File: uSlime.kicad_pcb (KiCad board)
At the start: 2 copper layers, 26.1 x 21.7 mm, 22 parts, among them U2 AP2112K-3.3TRG1, U3 MCP73831T-2ACI/OT, U4 ESP32-C6FH4, U5 BNO085

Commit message: Modify ESP32
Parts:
- removed U4: ESP32-C6FH4, uSlime-libs:QFN32_ESP32_EXP
- added J1: USB_C_4-LAYER_PADS, Connector_USB:USB_Micro-B_Amphenol_10103594-0001LF_Horizontal, F.Cu at (119.9, 113.9)
- added U1: ESP32-C6-WROOM-1-NARROW, PCM_Espressif:ESP32-C6-MINI-1, F.Cu at (111.8, 92.8)
- BOOT1, RESET1: value MOMENTARY-SWITCH-SPST-SMD-4.6X2.8MM -> SW_Push; footprint Button_Switch_SMD:SW_Push_1P1T_XKB_TS-1187A -> Button_Switch_SMD:SW_SPST_B3U-1000P-B
- moved R5 19.2 mm to (117.7, 105.3)
- moved R6 18.3 mm to (117.7, 107.3)
- moved R1 17.5 mm to (103.9, 96.5), turned to 90 degrees
- moved C3 16.2 mm to (120.6, 103.8)
- moved C2 16.1 mm to (110.4, 102.6)
- moved BOOT1 15.4 mm to (102.9, 92.3), turned to -90 degrees
- moved R3 15.3 mm to (113.2, 110.1)
- moved C4 14.9 mm to (120.7, 105.3)
- moved R4 14.7 mm to (113.2, 111.6)
- moved C5 10.9 mm to (110.2, 110.1)
- moved D1 9.06 mm to (117.4, 103.8), turned to 180 degrees
- moved RESET1 8.89 mm to (120.7, 92.3), turned to -90 degrees
- moved U2 7.86 mm to (119.2, 107.2)
- moved R8 5.97 mm to (104.1, 108.3), turned to 180 degrees
- moved R7 5.48 mm to (103.7, 104.6), turned to 180 degrees
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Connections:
- BOOT1 pad 2: GND -> /ESP32-C6FH4/IO9/BOOT
- C5 pad 2: Net-(U3-VBAT) -> unconnected-(C5-Pad2)
- D2 pad 2: Net-(D2-A) -> unconnected-(D2-A-Pad2)
- R1 pad 2: 3.3V -> +3.3V
- R3 pad 2: Net-(J1-CC2) -> unconnected-(R3-Pad2)
- R4 pad 2: Net-(J1-CC1) -> unconnected-(R4-Pad2)
- R8 pad 2: Net-(U3-STAT) -> unconnected-(R8-Pad2)
- RESET1 pad 2: GND -> /ESP32-C6FH4/ESP_EN
- U2 pad 3: Net-(D1-K) -> unconnected-(U2-EN-Pad3)
- U3 pad 1: Net-(U3-STAT) -> unconnected-(U3-STAT-Pad1)
- U3 pad 2: GND -> unconnected-(U3-VSS-Pad2)
- U3 pad 3: Net-(U3-VBAT) -> unconnected-(U3-VBAT-Pad3)
- U3 pad 4: Net-(D2-A) -> unconnected-(U3-VDD-Pad4)
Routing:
- net /ESP32-C6FH4/ESP_EN: track 0.00 -> 24.5 mm, vias 0 -> 2
- net /ESP32-C6FH4/IO9/BOOT: track 0.00 -> 15.4 mm
- net +3.3V: track 0.00 -> 4.51 mm
- net Net-(D1-A): track 0.00 -> 3.52 mm
- net /ESP32-C6FH4/IO8: track 0.00 -> 2.68 mm
- net Net-(D1-K): track 0.00 -> 1.95 mm
- net Net-(D2-K): track 0.00 -> 1.20 mm
- added copper zone on B.Cu, net GND
- added copper zone on F.Cu, net GND
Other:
- board size 26.1 x 21.7 mm -> 22.2 x 29.6 mm

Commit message: Update PCB
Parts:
- added C6: 0.1 uF, Capacitor_SMD:C_0603_1608Metric, B.Cu at (115.8, 92.1)
- added C7: 22pF, Capacitor_SMD:C_0603_1608Metric, B.Cu at (115.8, 94.6)
- added C8: 22pF, Capacitor_SMD:C_0603_1608Metric, B.Cu at (115.8, 97.1)
- added C9: 0.1 uF, Capacitor_SMD:C_0603_1608Metric, B.Cu at (115.8, 99.6)
- added Y1: 32.768, uSlime-libs:OSC-SMD_L3.2-W1.5, B.Cu at (111.7, 100.1)
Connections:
- U5 pad 10: unconnected-(U5-CLKSEL0-Pad10) -> GND
- U5 pad 11: unconnected-(U5-NRST-Pad11) -> BNO_RST
- U5 pad 17: unconnected-(U5-SA0/H_MOSI-Pad17) -> BNO_MOSI
- U5 pad 18: unconnected-(U5-H_CSN-Pad18) -> BNO_CS
- U5 pad 19: unconnected-(U5-H_SCL/SCK/RX-Pad19) -> BNO_SCL
- U5 pad 2: unconnected-(U5-GND-Pad2) -> GND
- U5 pad 20: unconnected-(U5-H_SDA/H_MISO/TX-Pad20) -> BNO_SDA
- U5 pad 25: unconnected-(U5-GND-Pad25) -> GND
- U5 pad 26: unconnected-(U5-XOUT32/CLKSEL1-Pad26) -> Net-(U5-XOUT32/CLKSEL1)
- U5 pad 27: unconnected-(U5-XIN32-Pad27) -> Net-(U5-XIN32)
- U5 pad 28: unconnected-(U5-VDDIO-Pad28) -> +3.3V
- U5 pad 3: unconnected-(U5-VDD-Pad3) -> +3.3V
- U5 pad 9: unconnected-(U5-CAP-Pad9) -> Net-(U5-CAP)

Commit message: update power
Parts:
- removed BOOT1: SW_Push, Button_Switch_SMD:SW_SPST_B3U-1000P-B
- added CHRG1: LED, LED_SMD:LED_0402_1005Metric, F.Cu at (102.9, 90.6)
- added U4: S2B-PH-K-S-GW, Connector_JST:JST_PH_S2B-PH-K_1x02_P2.00mm_Horizontal, F.Cu at (116.9, 112.2)
- added U6: MSK-12C02_SMD_SPDT_SWITCH, uSlime-libs:SW_PCM12SMTR, F.Cu at (128.9, 104.8)
- D1: footprint LED_SMD:LED_0402_1005Metric -> Diode_SMD:D_0603_1608Metric
- J1: value USB_C_4-LAYER_PADS -> USB_B_Micro
- R5: value 100k -> 390
- R6: value 390 -> 10K
- R7: value R -> 100K
- U5: moved to F.Cu
- moved U5 20.2 mm to (104.2, 114.3), turned to 0 degrees
- moved C1 7.50 mm to (129.2, 96.4)
- moved R2 7.50 mm to (127.2, 96.4)
- moved RESET1 7.50 mm to (128.2, 92.2)
- moved J1 6.69 mm to (126.5, 114.8)
- moved R6 4.57 mm to (120.4, 103.6)
- moved C5 3.95 mm to (108.9, 106.3)
- moved R3 3.95 mm to (111.9, 106.3)
- moved R4 3.95 mm to (111.9, 107.8)
- moved R5 1.28 mm to (117.4, 106.6)
- moved C4 1.28 mm to (120.4, 106.6)
- moved C3 1.27 mm to (120.4, 105.1)
- moved D1 1.25 mm to (117.4, 105.1)
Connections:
- C3 pad 1: Net-(D1-K) -> VBAT
- C4 pad 1: Net-(U2-VOUT) -> 3.3V
- C5 pad 1: unconnected-(C5-Pad1) -> GND
- C5 pad 2: unconnected-(C5-Pad2) -> VBAT
- C6 pad 1: unconnected-(C6-Pad1) -> GND
- D1 pad 1: Net-(D1-K) -> VBAT
- D1 pad 2: Net-(D1-A) -> VBUS
- J1 pad 1: V_USB -> VBUS
- J1 pad 2: /ESP32-C6FH4/USB_N -> D+ P
- J1 pad 3: /ESP32-C6FH4/USB_P -> D- N
- R5 pad 1: Net-(D1-A) -> VBUS
- R6 pad 1: Net-(D1-A) -> VBAT
- R6 pad 2: unconnected-(R6-Pad2) -> GND
- R7 pad 1: GND -> VBUS
- R7 pad 2: unconnected-(R7-Pad2) -> GND
- R8 pad 1: Net-(D2-K) -> Net-(CHRG1-K)
- R8 pad 2: unconnected-(R8-Pad2) -> Net-(U3-STAT)
- U1 pad 13: /ESP32-C6FH4/USB_N -> D- N
- U1 pad 14: /ESP32-C6FH4/USB_P -> D+ P
- U2 pad 1: Net-(D1-K) -> VBAT
- U2 pad 3: unconnected-(U2-EN-Pad3) -> VBAT
- U2 pad 5: Net-(U2-VOUT) -> 3.3V
- U3 pad 1: unconnected-(U3-STAT-Pad1) -> Net-(U3-STAT)
- U3 pad 2: unconnected-(U3-VSS-Pad2) -> GND
- U3 pad 3: unconnected-(U3-VBAT-Pad3) -> VBAT
- U3 pad 4: unconnected-(U3-VDD-Pad4) -> VBUS
- U3 pad 5: unconnected-(U3-PROG-Pad5) -> Net-(U3-PROG)
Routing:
- net /ESP32-C6FH4/IO9/BOOT: track 15.4 -> 2.26 mm
- net Net-(D1-A): track 3.52 -> 0.00 mm
- net VBAT: track 0.00 -> 1.95 mm
- net Net-(D1-K): track 1.95 -> 0.00 mm
- net VBUS: track 0.00 -> 1.52 mm
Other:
- board size 22.2 x 29.6 mm -> 30 x 30 mm

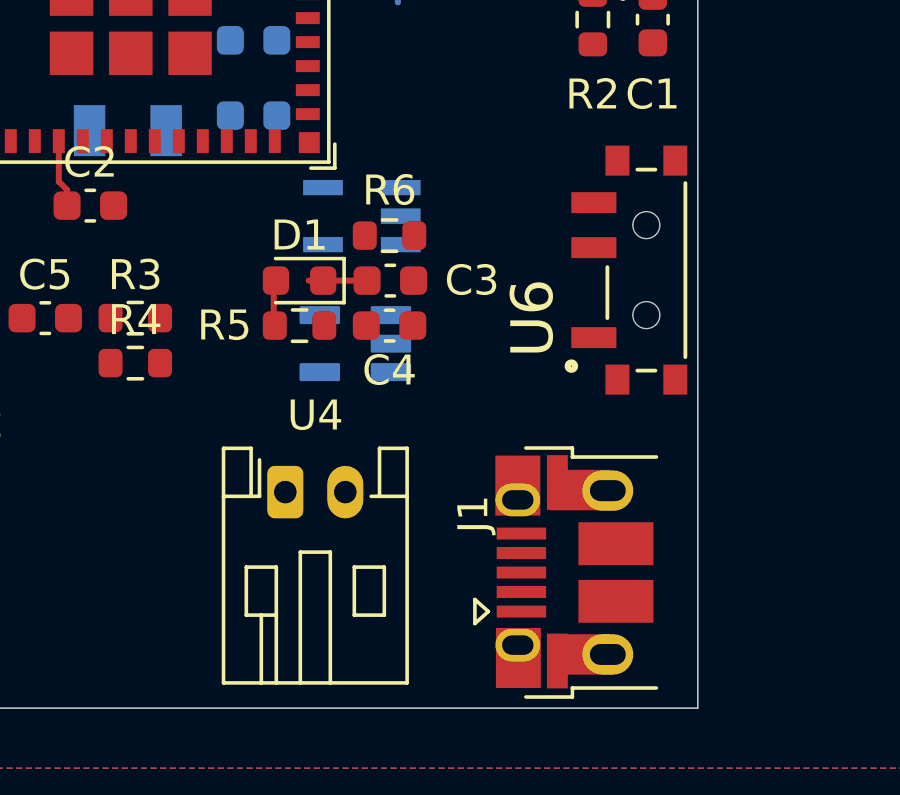
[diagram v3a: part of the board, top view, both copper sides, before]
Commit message: Modify ESP32 connections
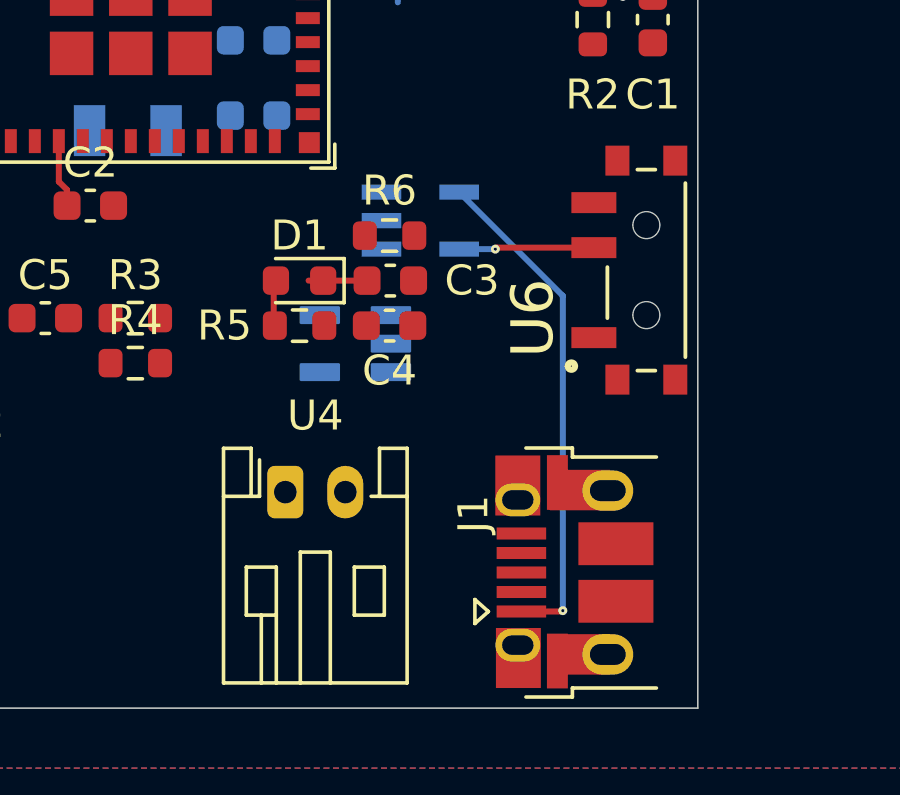
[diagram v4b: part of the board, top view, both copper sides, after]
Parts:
- moved U3 1.96 mm to (121.4, 103.1), turned to 0 degrees
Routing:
- net VBUS: track 1.52 -> 18.3 mm, vias 0 -> 1
- net Net-(U3-PROG): track 0.00 -> 4.51 mm, vias 0 -> 1

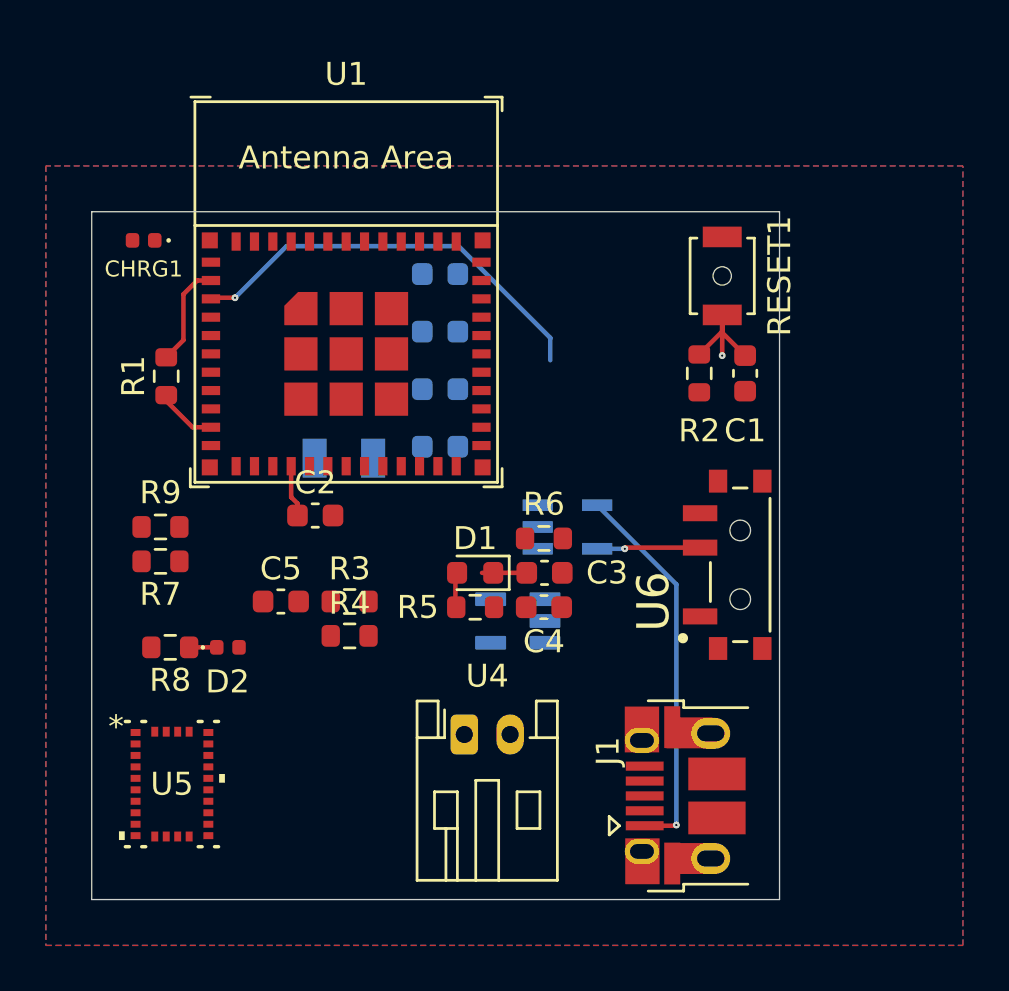
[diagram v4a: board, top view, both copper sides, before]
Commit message: Replace ESP32 symbol with right ESP32
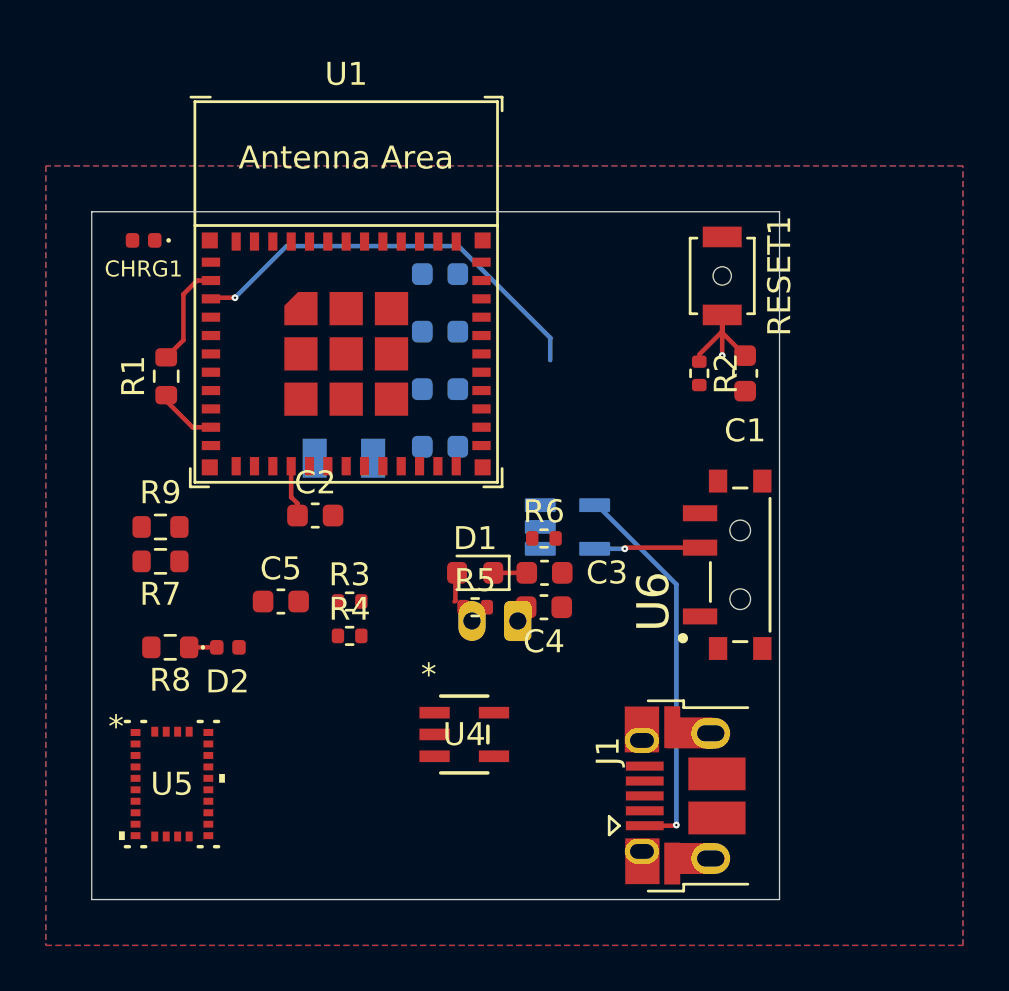
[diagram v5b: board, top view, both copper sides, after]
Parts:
- R2: footprint Resistor_SMD:R_0603_1608Metric -> Resistor_SMD:R_0402_1005Metric
- R3: value 5.1k -> 100K; footprint Resistor_SMD:R_0603_1608Metric -> Resistor_SMD:R_0402_1005Metric
- R4: value 5.1k -> 1k; footprint Resistor_SMD:R_0603_1608Metric -> Resistor_SMD:R_0402_1005Metric
- R5: value 390 -> 4.7k; footprint Resistor_SMD:R_0603_1608Metric -> Resistor_SMD:R_0402_1005Metric
- R6: value 10K -> 100KOHM-0402T-1/16W-1%; footprint Resistor_SMD:R_0603_1608Metric -> Resistor_SMD:R_0402_1005Metric
- U1: value ESP32-C6-WROOM-1-NARROW -> ESP32-C6-MINI-1
- U2: value AP2112K-3.3TRG1 -> S2B-PH-K-S-GW; footprint uSlime-libs:SOT95P285X140-5N -> Connector_JST:JST_PH_S2B-PH-K_1x02_P2.00mm_Horizontal
- U3: value MCP73831T-2ACI/OT -> AP2112K-3.3TRG1; footprint uSlime-libs:SOT-23-5_MC_MCH -> uSlime-libs:SOT95P285X140-5N
- U4: value S2B-PH-K-S-GW -> MCP73831T-2ACI/OT; footprint Connector_JST:JST_PH_S2B-PH-K_1x02_P2.00mm_Horizontal -> uSlime-libs:SOT-23-5_MC_MCH
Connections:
- C4 pad 1: 3.3V -> +3.3V
- R2 pad 2: 3.3V -> +3.3V
- R3 pad 1: GND -> VBUS
- R3 pad 2: unconnected-(R3-Pad2) -> GND
- R4 pad 1: GND -> Net-(CHRG1-K)
- R4 pad 2: unconnected-(R4-Pad2) -> Net-(U4-STAT)
- R5 pad 1: VBUS -> GND
- R5 pad 2: GND -> unconnected-(R5-Pad2)
- R6 pad 1: VBAT -> /ESP32-C6FH4/IO8
- R6 pad 2: GND -> +3.3V
- U1 pad 10: /ESP32-C6FH4/IO8 -> /ESP32-C6FH4/IO5
- U1 pad 11: /ESP32-C6FH4/IO10 -> GND
- U1 pad 12: /ESP32-C6FH4/IO11/~{ALRT} -> /ESP32-C6FH4/IO0
- U1 pad 13: D- N -> /ESP32-C6FH4/IO1/V_BATT_2
- U1 pad 14: D+ P -> GND
- U1 pad 15: /ESP32-C6FH4/IO9/BOOT -> BNO_SDA
- U1 pad 16: /ESP32-C6FH4/IO18/~{CS} -> BNO_SCL
- U1 pad 17: /ESP32-C6FH4/IO19/SCK -> D- N
- U1 pad 18: /ESP32-C6FH4/IO20/PICO -> D+ P
- U1 pad 19: /ESP32-C6FH4/IO21/POCI -> /ESP32-C6FH4/IO14
- U1 pad 2: +3.3V -> GND
- U1 pad 20: /ESP32-C6FH4/IO22/~{SD_DET} -> /ESP32-C6FH4/IO15/LP
- U1 pad 21: /ESP32-C6FH4/IO23/STAT -> (no net)
- U1 pad 22: (no net) -> /ESP32-C6FH4/IO8
- U1 pad 23: /ESP32-C6FH4/IO15/LP -> /ESP32-C6FH4/IO9/BOOT
- U1 pad 24: /ESP32-C6FH4/IO17/RX -> BNO_CS
- U1 pad 25: /ESP32-C6FH4/IO16/TX -> BNO_MOSI
- U1 pad 26: /ESP32-C6FH4/IO3 -> /ESP32-C6FH4/IO20/PICO
- U1 pad 27: /ESP32-C6FH4/IO2 -> /ESP32-C6FH4/IO21/POCI
- U1 pad 28: GND -> /ESP32-C6FH4/IO22/~{SD_DET}
- U1 pad 29: GND -> /ESP32-C6FH4/IO23/STAT
- U1 pad 3: /ESP32-C6FH4/ESP_EN -> +3.3V
- U1 pad 30: GND -> /ESP32-C6FH4/IO17/RX
- U1 pad 31: GND -> /ESP32-C6FH4/IO16/TX
- U1 pad 32: GND -> (no net)
- U1 pad 33: GND -> (no net)
- U1 pad 34: GND -> (no net)
- U1 pad 35: GND -> (no net)
- U1 pad 38: (no net) -> GND
- U1 pad 39: (no net) -> GND
- U1 pad 4: /ESP32-C6FH4/IO4 -> (no net)
- U1 pad 40: (no net) -> GND
- U1 pad 41: (no net) -> GND
- U1 pad 42: (no net) -> GND
- U1 pad 43: (no net) -> GND
- U1 pad 44: (no net) -> GND
- U1 pad 45: (no net) -> GND
- U1 pad 46: (no net) -> GND
- U1 pad 47: (no net) -> GND
- U1 pad 48: (no net) -> GND
- U1 pad 49: (no net) -> GND
- U1 pad 5: /ESP32-C6FH4/IO5 -> /ESP32-C6FH4/IO2
- U1 pad 50: (no net) -> GND
- U1 pad 51: (no net) -> GND
- U1 pad 52: (no net) -> GND
- U1 pad 53: (no net) -> GND
- U1 pad 6: /ESP32-C6FH4/IO6/SDA -> /ESP32-C6FH4/IO3
- U1 pad 7: /ESP32-C6FH4/IO7/SCL -> (no net)
- U1 pad 8: /ESP32-C6FH4/IO0 -> /ESP32-C6FH4/ESP_EN
- U1 pad 9: /ESP32-C6FH4/IO1 -> /ESP32-C6FH4/IO4
- U3 pad 1: Net-(U3-STAT) -> VBAT
- U3 pad 4: VBUS -> (no net)
- U3 pad 5: Net-(U3-PROG) -> +3.3V
- U4 pad 1: VBAT -> Net-(U4-STAT)
- U6 pad COM: Net-(U3-PROG) -> Net-(U4-PROG)
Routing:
- net /ESP32-C6FH4/ESP_EN: track 24.5 -> 6.10 mm, vias 2 -> 1
- net +3.3V: track 4.51 -> 22.9 mm, vias 0 -> 1
- net Net-(U3-PROG): track 4.51 -> 0.00 mm, vias 1 -> 0
- net (no net): track 0.00 -> 4.51 mm
- net Net-(U4-PROG): vias 0 -> 1

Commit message: PCB Smol Time
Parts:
- removed D2: LED, LED_SMD:LED_0402_1005Metric
- removed R6: 100KOHM-0402T-1/16W-1%, Resistor_SMD:R_0402_1005Metric
- removed R7: 100K, Resistor_SMD:R_0603_1608Metric
- removed R8: 1k, Resistor_SMD:R_0603_1608Metric
- removed R9: 4.7k, Resistor_SMD:R_0603_1608Metric
- C1, C2, C3, C4, C5: footprint Capacitor_SMD:C_0603_1608Metric -> Capacitor_SMD:C_0402_1005Metric
- C6, C7, C8, C9: footprint Capacitor_SMD:C_0603_1608Metric -> Capacitor_SMD:C_0402_1005Metric; moved to F.Cu
- R1: value 100KOHM-0603-1/10W-1% -> 100KOHM-0402T-1/16W-1%; footprint Resistor_SMD:R_0603_1608Metric -> Resistor_SMD:R_0402_1005Metric
- U2, U3, Y1: moved to F.Cu
- moved C6 21.8 mm to (102.2, 109.1), turned to 90 degrees
- moved CHRG1 21.1 mm to (114.4, 108.3), turned to 0 degrees
- moved R2 19.8 mm to (108.5, 102.8)
- moved C8 15.1 mm to (101.9, 102.8), turned to 90 degrees
- moved J1 14.0 mm to (119.5, 102.8)
- moved U6 13.6 mm to (120.8, 93.8)
- moved C1 13.0 mm to (116.2, 95.6)
- moved U2 12.9 mm to (107.5, 112.3), turned to -90 degrees
- moved C7 11.8 mm to (107.4, 102.8), turned to 90 degrees
- moved RESET1 11.6 mm to (116.5, 92.0)
- moved U3 10.3 mm to (111.2, 104.1), turned to 180 degrees
- moved C9 9.40 mm to (108.5, 105.4), turned to -90 degrees
- moved R5 9.28 mm to (118.2, 97.3)
- moved R1 8.86 mm to (111.0, 101.8), turned to 180 degrees
- moved U4 7.75 mm to (110.2, 108.3), turned to 180 degrees
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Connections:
- R5 pad 2: unconnected-(R5-Pad2) -> Net-(R5-Pad2)
- U1 pad 5: /ESP32-C6FH4/IO2 -> BNO_INT
- U1 pad 6: /ESP32-C6FH4/IO3 -> BNO_RST
- U5 pad 14: unconnected-(U5-H_INTN-Pad14) -> BNO_INT
- U6 pad L1: unconnected-(U6-PadL1) -> VBUS
- U6 pad L2: unconnected-(U6-PadL2) -> Net-(R5-Pad2)
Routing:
- net GND: track 0.00 -> 32.8 mm, vias 0 -> 8
- net Net-(U4-PROG): track 0.00 -> 28.1 mm, vias 1 -> 2
- net BNO_INT: track 0.00 -> 18.8 mm, vias 0 -> 2
- net /ESP32-C6FH4/ESP_EN: track 6.10 -> 23.7 mm, vias 1 -> 4
- net BNO_RST: track 0.00 -> 16.9 mm, vias 0 -> 2
- net VBUS: track 18.3 -> 35.1 mm, vias 1 -> 4
- net VBAT: track 1.95 -> 18.5 mm
- net D- N: track 0.00 -> 15.4 mm, vias 0 -> 2
- net BNO_MOSI: track 0.00 -> 14.9 mm, vias 0 -> 2
- net D+ P: track 0.00 -> 14.6 mm, vias 0 -> 2
- net BNO_CS: track 0.00 -> 14.3 mm, vias 0 -> 2
- net +3.3V: track 22.9 -> 37.0 mm, vias 1 -> 6
- net BNO_SCL: track 0.00 -> 13.3 mm, vias 0 -> 2
- net BNO_SDA: track 0.00 -> 10.4 mm, vias 0 -> 2
- net (no net): track 4.51 -> 0.00 mm
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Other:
- board size 30 x 30 mm -> 21.9 x 27.5 mm
